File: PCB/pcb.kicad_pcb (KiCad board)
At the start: 2 copper layers, 404.8 x 127 mm, 324 parts, among them J1 USB_C_Receptacle_USB2.0, SW1 SW_Push, U1 AT90USB1286-AU, Y1 Crystal_GND24_Small

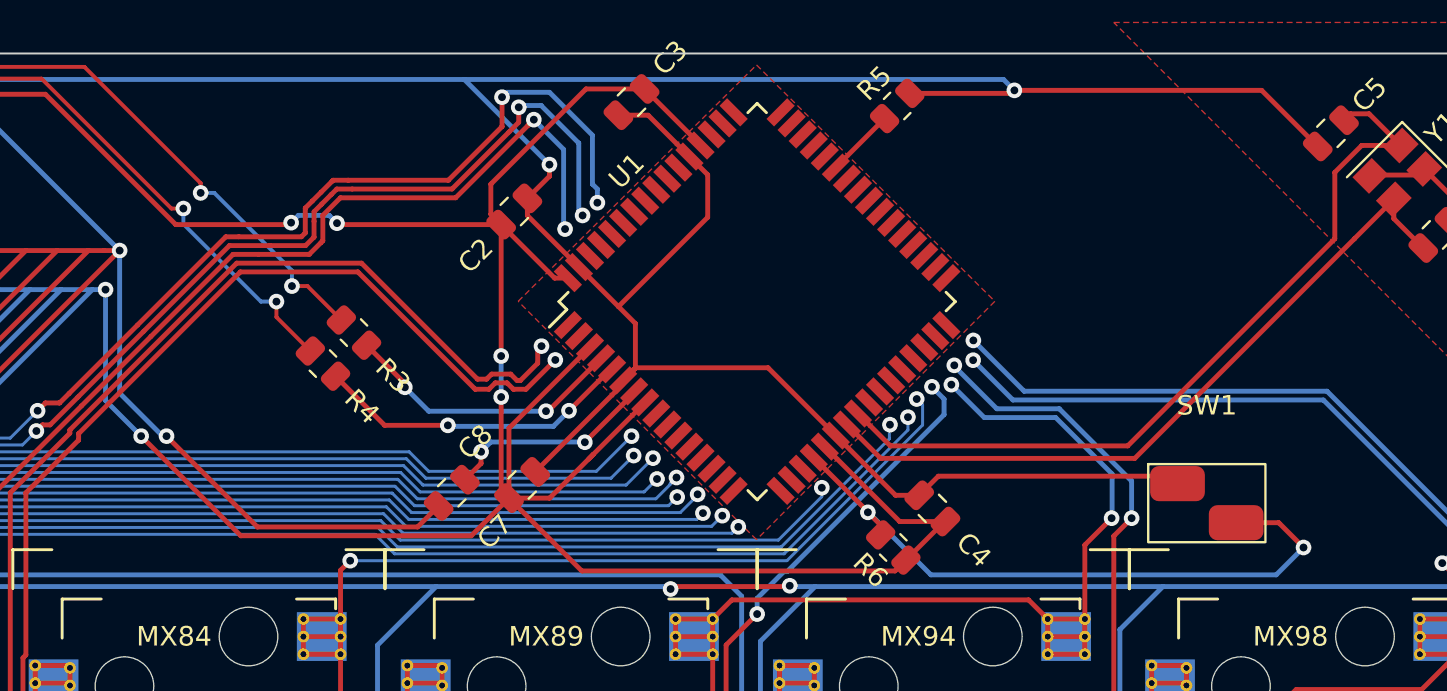
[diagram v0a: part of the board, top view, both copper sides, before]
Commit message: All Rows and Columns connected
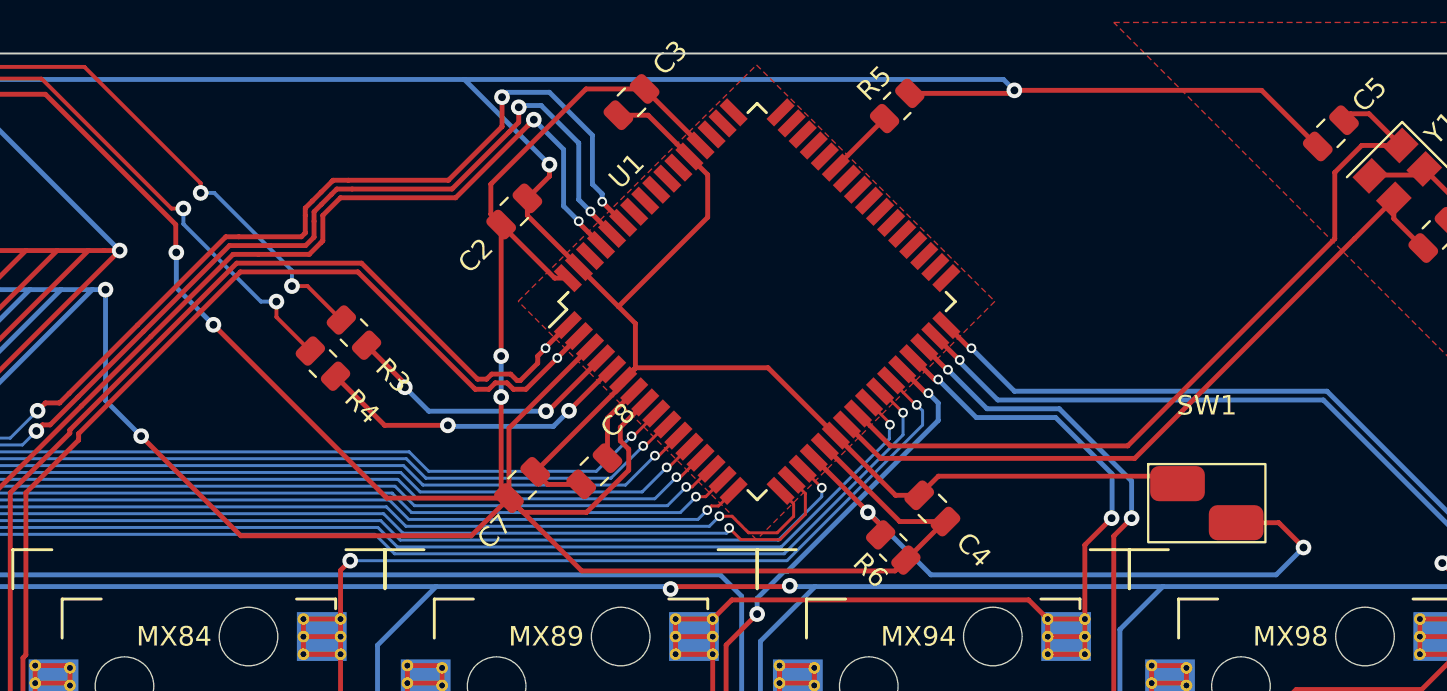
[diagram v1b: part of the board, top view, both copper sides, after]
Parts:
- moved C8 7.38 mm to (444.9, 184.9)
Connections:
- U1 pad 1: unconnected-(U1-Pad1) -> ROW3
- U1 pad 10: unconnected-(U1-Pad10) -> COL3
- U1 pad 11: unconnected-(U1-Pad11) -> COL4
- U1 pad 12: unconnected-(U1-Pad12) -> COL5
- U1 pad 13: unconnected-(U1-Pad13) -> COL6
- U1 pad 14: unconnected-(U1-Pad14) -> COL7
- U1 pad 15: unconnected-(U1-Pad15) -> COL8
- U1 pad 16: unconnected-(U1-Pad16) -> COL9
- U1 pad 17: unconnected-(U1-Pad17) -> COL10
- U1 pad 18: unconnected-(U1-Pad18) -> COL11
- U1 pad 19: unconnected-(U1-Pad19) -> COL12
- U1 pad 2: unconnected-(U1-Pad2) -> ROW1
- U1 pad 25: unconnected-(U1-Pad25) -> COL13
- U1 pad 26: unconnected-(U1-Pad26) -> COL14
- U1 pad 27: unconnected-(U1-Pad27) -> COL15
- U1 pad 28: unconnected-(U1-Pad28) -> ROW2
- U1 pad 29: unconnected-(U1-Pad29) -> COL16
- U1 pad 30: unconnected-(U1-Pad30) -> ROW0
- U1 pad 31: unconnected-(U1-Pad31) -> COL17
- U1 pad 32: unconnected-(U1-Pad32) -> ROW5
- U1 pad 59: unconnected-(U1-Pad59) -> COL0
- U1 pad 60: unconnected-(U1-Pad60) -> COL1
- U1 pad 61: unconnected-(U1-Pad61) -> ROW4
- U1 pad 9: unconnected-(U1-Pad9) -> COL2
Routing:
- net GND: track 4824.2 -> 4799.9 mm, vias 23 -> 22
- net +5V: track 3578.0 -> 3587.9 mm
- net Net-(C8-Pad1): track 10.9 -> 4.05 mm, vias 2 -> 0
- net COL11: track 297.7 -> 304.0 mm
- net COL10: track 324.0 -> 329.9 mm
- net COL16: track 170.4 -> 172.9 mm
- net COL17: track 107.5 -> 110.0 mm
- net COL3: track 411.7 -> 414.0 mm
- net COL7: track 654.6 -> 656.9 mm
- net COL5: track 755.0 -> 757.3 mm
- net COL9: track 341.6 -> 343.6 mm
- net ROW0: track 442.7 -> 444.6 mm
- net COL4: track 393.7 -> 395.5 mm
- net COL14: track 215.2 -> 217.0 mm
- net COL2: track 458.9 -> 460.6 mm
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
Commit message: LED Data Bus connected
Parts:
- SW1: footprint led:switch_without_switch -> random-keyboard-parts:SKQG-1155865
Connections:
- U1 pad 51: unconnected-(U1-Pad51) -> RGBDIN
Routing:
- net RGBDIN: track 0.00 -> 386.1 mm, vias 0 -> 5
- net GND: track 4799.9 -> 4837.4 mm
- net Net-(C6-Pad1): track 37.3 -> 0.00 mm
- net ROW4: track 474.5 -> 473.8 mm
- net COL1: track 463.8 -> 463.1 mm
- net COL0: track 503.7 -> 502.9 mm
- net COL12: track 284.4 -> 283.7 mm
- net COL13: track 248.4 -> 247.8 mm

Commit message: Reset Switch Footprint Updated
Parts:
- D21: footprint led:D_SOD-123 -> led:switch_without_switch
- SW1: footprint random-keyboard-parts:SKQG-1155865 -> led:switch_without_switch
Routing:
- net GND: track 4837.4 -> 4800.1 mm
- net Net-(C6-Pad1): track 0.00 -> 37.3 mm

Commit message: Silkscreen Legends updated
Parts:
- D21: footprint led:switch_without_switch -> led:D_SOD-123
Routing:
- added copper zone on B.Cu, net GND
